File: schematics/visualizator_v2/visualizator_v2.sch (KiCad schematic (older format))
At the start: 20 parts, among them J1 5V, J2 WS2812, J3 Audio, SW1 COLOR, SW2 PATTERN, U1 ATmega328-16PU, Y1 16MHz

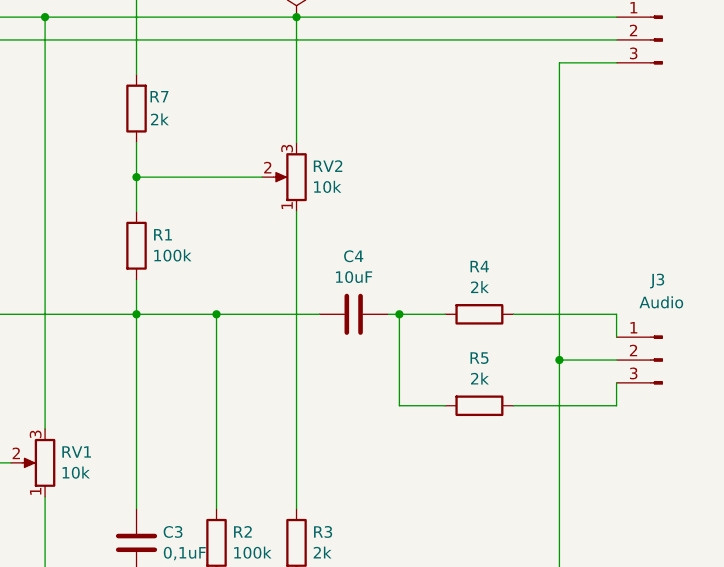
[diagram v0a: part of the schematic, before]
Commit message: Changed reistors
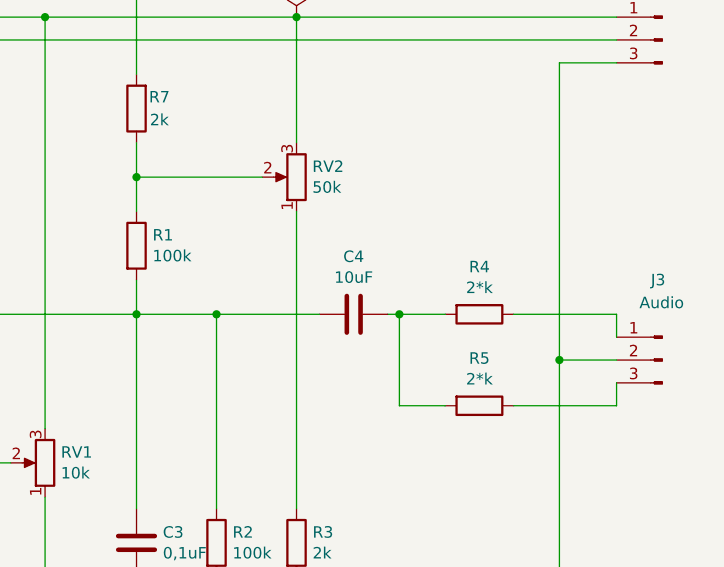
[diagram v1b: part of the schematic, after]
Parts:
- R4, R5: value 2k -> 2*k
- RV2: value 10k -> 50k
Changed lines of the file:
@@
 P 7750 2400
 F 0 "RV2" H 7681 2354 50  0000 R CNN
-F 1 "10k" H 7681 2445 50  0000 R CNN
+F 1 "50k" H 7681 2445 50  0000 R CNN
 F 2 "Potentiometer_THT:Potentiometer_Alps_RK09K_Single_Vertical" H 7750 2400 50  0001 C CNN
 F 3 "~" H 7750 2400 50  0001 C CNN
@@
 P 8550 3000
 F 0 "R4" V 8343 3000 50  0000 C CNN
-F 1 "2k" V 8434 3000 50  0000 C CNN
+F 1 "2*k" V 8434 3000 50  0000 C CNN
 F 2 "Resistor_THT:R_Axial_DIN0207_L6.3mm_D2.5mm_P10.16mm_Horizontal" V 8480 3000 50  0001 C CNN
 F 3 "~" H 8550 3000 50  0001 C CNN
@@
 P 8550 3400
 F 0 "R5" V 8343 3400 50  0000 C CNN
-F 1 "2k" V 8434 3400 50  0000 C CNN
+F 1 "2*k" V 8434 3400 50  0000 C CNN
 F 2 "Resistor_THT:R_Axial_DIN0207_L6.3mm_D2.5mm_P10.16mm_Horizontal" V 8480 3400 50  0001 C CNN
 F 3 "~" H 8550 3400 50  0001 C CNN
